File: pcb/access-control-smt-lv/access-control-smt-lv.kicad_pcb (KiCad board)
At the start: 2 copper layers, 65.9 x 33.8 mm, 36 parts, among them U1 ESP32-WROOM-E

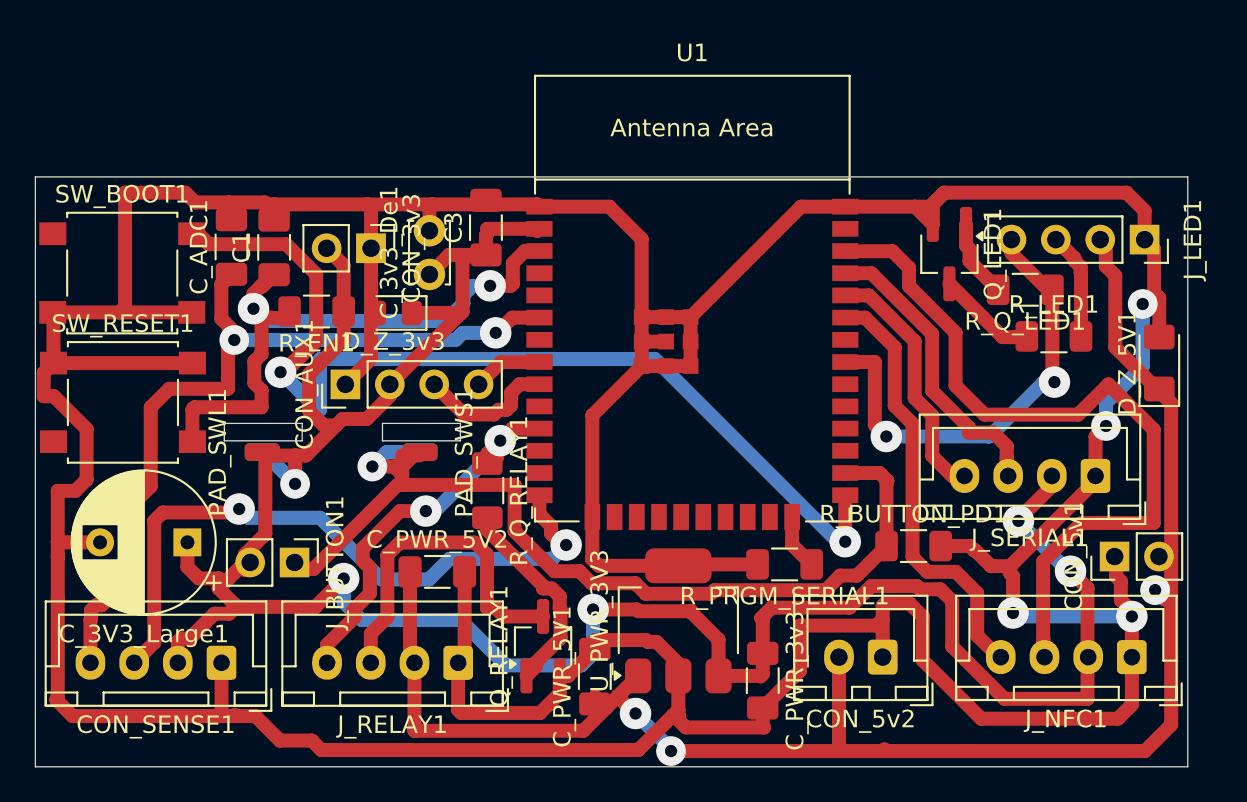
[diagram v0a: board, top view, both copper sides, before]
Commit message: Silkscreen updates with version, date and logo
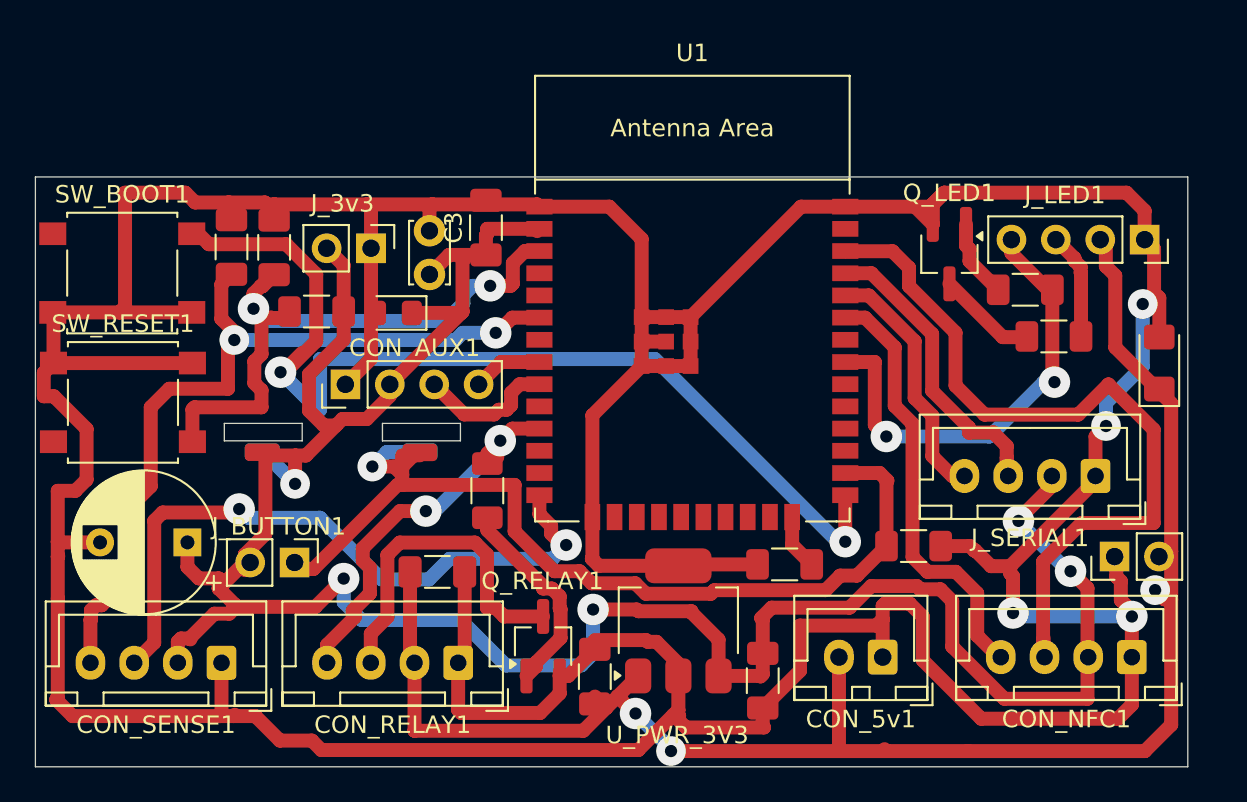
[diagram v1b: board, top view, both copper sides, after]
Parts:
- renumbered CON_5v2 to CON_5v1, J_NFC1 to CON_NFC1, J_RELAY1 to CON_RELAY1, CON_3v3 to J_3v3, CON_5v1 to J_5v1
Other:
- board text added: "access-control-smt-lv V1.0 2025-05-16"

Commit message: Final changes pre manufacture
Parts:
- added R_I2C_PU1: 10kR, Resistor_SMD:R_1206_3216Metric_Pad1.30x1.75mm_HandSolder, B.Cu at (39.9, 8.24)
- added R_I2C_PU2: 10kR, Resistor_SMD:R_1206_3216Metric_Pad1.30x1.75mm_HandSolder, B.Cu at (35.5, 12.4)
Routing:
- net +3V3: track 150.9 -> 167.3 mm, vias 5 -> 6
- net Net-(CON_NFC1-Pin_4): track 24.7 -> 39.4 mm, vias 0 -> 1
- net GND: track 324.5 -> 337.2 mm, vias 4 -> 8
- net Net-(CON_NFC1-Pin_3): track 44.8 -> 54.9 mm, vias 0 -> 1
- net Net-(U1-GPIO0/BOOT/ADC2_CH1): track 59.1 -> 55.6 mm
- added copper zone on B.Cu, net GND
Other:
- board text added: "access-control-smt-lv V1.0 2025-05-20"
- board text removed: "access-control-smt-lv V1.0 2025-05-16"
